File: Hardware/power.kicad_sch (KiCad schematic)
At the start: 20 parts, among them U3 LM66200DRLR, U4 MAX77827AEFD+T, U5 SC4215

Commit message: Updated SD card, GPIOs, CAN, Power section
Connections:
- net RBUS_uC_V: now also U3.6 (VIN2); no longer U3.3 (VIN1)
- net VBUS: now also U3.3 (VIN1); no longer U3.6 (VIN2)
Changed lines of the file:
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@@
+	(wire
+		(pts
+			(xy 34.544 41.91) (xy 46.99 41.91)
+		)
+		(stroke
+			(width 0)
+			(type default)
+		)
+	)
 	(wire
 		(pts
@@
 	(wire
 		(pts
+			(xy 80.01 41.91) (xy 93.726 41.91)
+		)
+		(stroke
+			(width 0)
+			(type default)
+		)
+	)
+	(wire
+		(pts
 			(xy 171.45 64.77) (xy 166.37 64.77)
 		)
@@
 	(wire
 		(pts
-			(xy 34.29 41.91) (xy 46.99 41.91)
-		)
-		(stroke
-			(width 0)
-			(type default)
-		)
-	)
-	(wire
-		(pts
 			(xy 101.6 52.07) (xy 123.19 52.07)
 		)
@@
 	(wire
 		(pts
-			(xy 90.17 39.37) (xy 80.01 39.37)
-		)
-		(stroke
-			(width 0)
-			(type default)
-		)
-	)
-	(wire
-		(pts
 			(xy 240.03 60.96) (xy 240.03 62.23)
 		)
@@
 	)
 	(label "VoutDiode"
-		(at 80.01 41.91 0)
+		(at 93.726 41.91 0)
 		(effects
 			(font
@@
 	(global_label "RBUS_uC_V"
 		(shape input)
-		(at 34.29 41.91 180)
+		(at 80.01 39.37 0)
 		(fields_autoplaced yes)
 		(effects
@@
 				(size 1.27 1.27)
 			)
-			(justify right)
+			(justify left)
 		)
 		(property "Intersheetrefs" "${INTERSHEET_REFS}"
-			(at 21.4362 41.91 0)
-			(effects
-				(font
-					(size 1.27 1.27)
-				)
-				(justify right)
+			(at 92.8638 39.37 0)
+			(effects
+				(font
+					(size 1.27 1.27)
+				)
+				(justify left)
 				(hide yes)
 			)
@@
 	(symbol
 		(lib_id "power:VBUS")
-		(at 90.17 39.37 0)
+		(at 34.544 41.91 0)
 		(unit 1)
 		(exclude_from_sim no)
@@
 		(fields_autoplaced yes)
 		(property "Reference" "#PWR044"
-			(at 90.17 43.18 0)
+			(at 34.544 45.72 0)
 			(effects
 				(font
@@
 		)
 		(property "Value" "VBUS"
-			(at 90.17 35.7942 0)
+			(at 34.544 38.3342 0)
 			(effects
 				(font
@@
 		)
 		(property "Footprint" ""
-			(at 90.17 39.37 0)
+			(at 34.544 41.91 0)
 			(effects
 				(font
@@
 		)
 		(property "Datasheet" ""
-			(at 90.17 39.37 0)
+			(at 34.544 41.91 0)
 			(effects
 				(font
@@
 		)
 		(property "Description" ""
-			(at 90.17 39.37 0)
-			(effects
-				(font
+			(at 34.544 41.91 0)
+			(effects
+				(font

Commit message: Most Review Changes
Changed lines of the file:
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@@
 	(text "Be extra careful in leaving this connected at a single point\n"
 		(exclude_from_sim no)
-		(at 125.73 116.84 0)
+		(at 123.19 90.678 0)
 		(effects
 			(font
@@
 	(wire
 		(pts
-			(xy 153.67 119.38) (xy 158.75 119.38)
+			(xy 151.13 93.218) (xy 156.21 93.218)
 		)
 		(stroke
@@
 	)
 	(label "GNDA"
-		(at 153.67 119.38 180)
+		(at 151.13 93.218 180)
 		(effects
 			(font
@@
 	(symbol
 		(lib_id "power:GND")
-		(at 158.75 119.38 0)
+		(at 156.21 93.218 0)
 		(unit 1)
 		(exclude_from_sim no)
@@
 		(fields_autoplaced yes)
 		(property "Reference" "#PWR050"
-			(at 158.75 125.73 0)
+			(at 156.21 99.568 0)
 			(effects
 				(font
@@
 		)
 		(property "Value" "GND"
-			(at 158.75 123.8234 0)
+			(at 156.21 97.6614 0)
 			(effects
 				(font
@@
 		)
 		(property "Footprint" ""
-			(at 158.75 119.38 0)
+			(at 156.21 93.218 0)
 			(effects
 				(font
@@
 		)
 		(property "Datasheet" ""
-			(at 158.75 119.38 0)
+			(at 156.21 93.218 0)
 			(effects
 				(font
@@
 		)
 		(property "Description" ""
-			(at 158.75 119.38 0)
+			(at 156.21 93.218 0)
 			(effects
 				(font

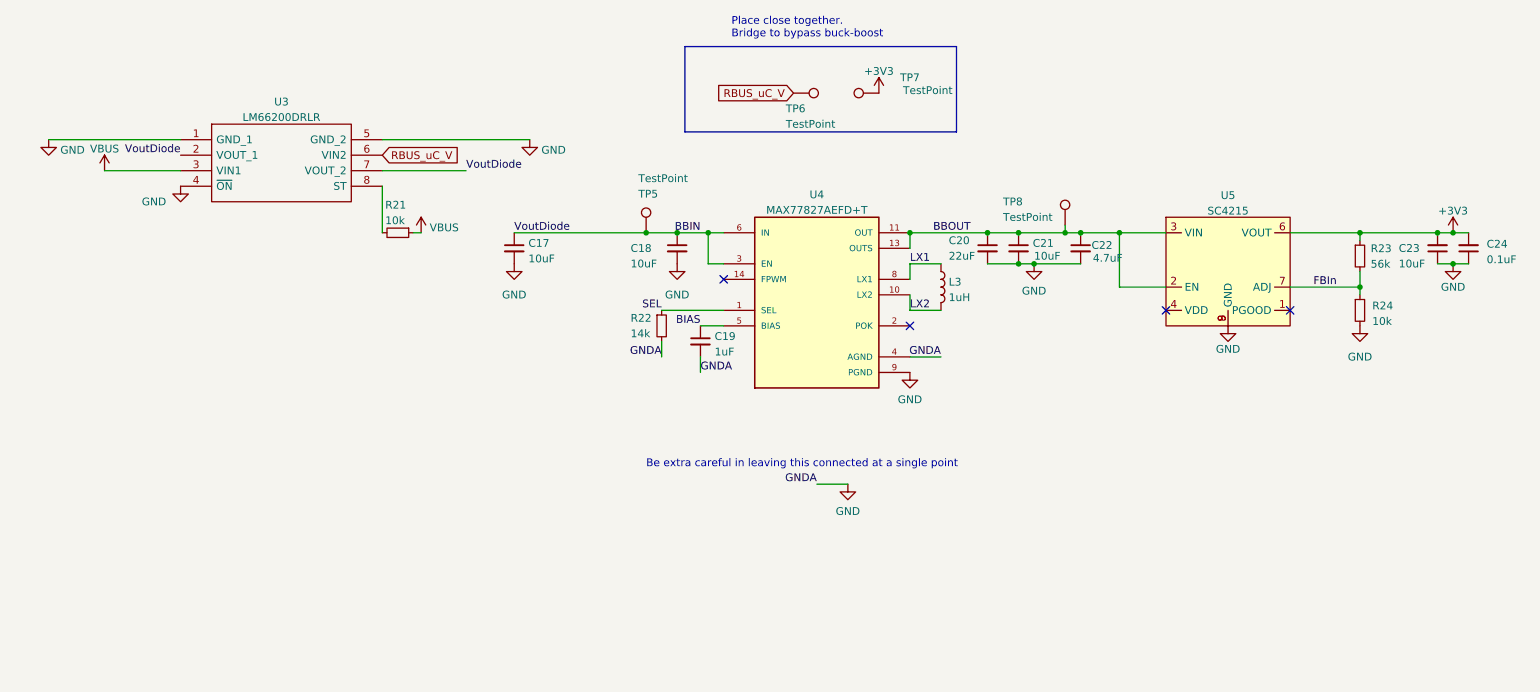
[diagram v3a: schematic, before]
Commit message: schematic reformatting and bom consolidation
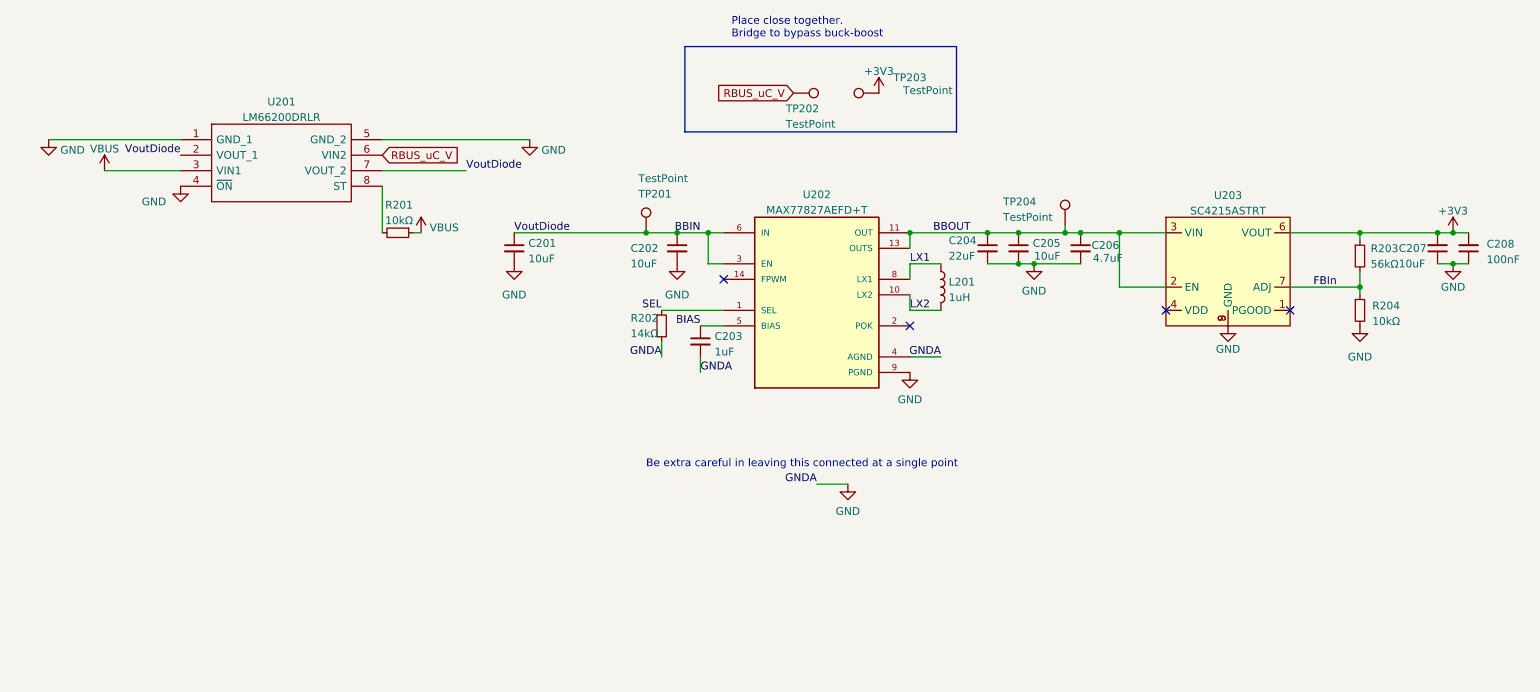
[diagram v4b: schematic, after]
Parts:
- C208: renamed from C24; value 0.1uF -> 100nF
- R201: renamed from R21; value 10k -> 10kΩ
- R202: renamed from R22; value 14k -> 14kΩ
- R203: renamed from R23; value 56k -> 56kΩ
- R204: renamed from R24; value 10k -> 10kΩ
- TP201: renamed from TP5; now left out of the parts list
- TP202: renamed from TP6; now left out of the parts list
- TP203: renamed from TP7; now left out of the parts list
- TP204: renamed from TP8; now left out of the parts list
- U203: renamed from U5; value SC4215 -> SC4215ASTRT
- renumbered C17 to C201, C18 to C202, C19 to C203, C20 to C204, C21 to C205, C22 to C206, C23 to C207, L3 to L201, U3 to U201, U4 to U202
